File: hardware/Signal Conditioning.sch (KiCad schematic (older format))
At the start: 22 parts, among them U2 LM324, U3 LM324

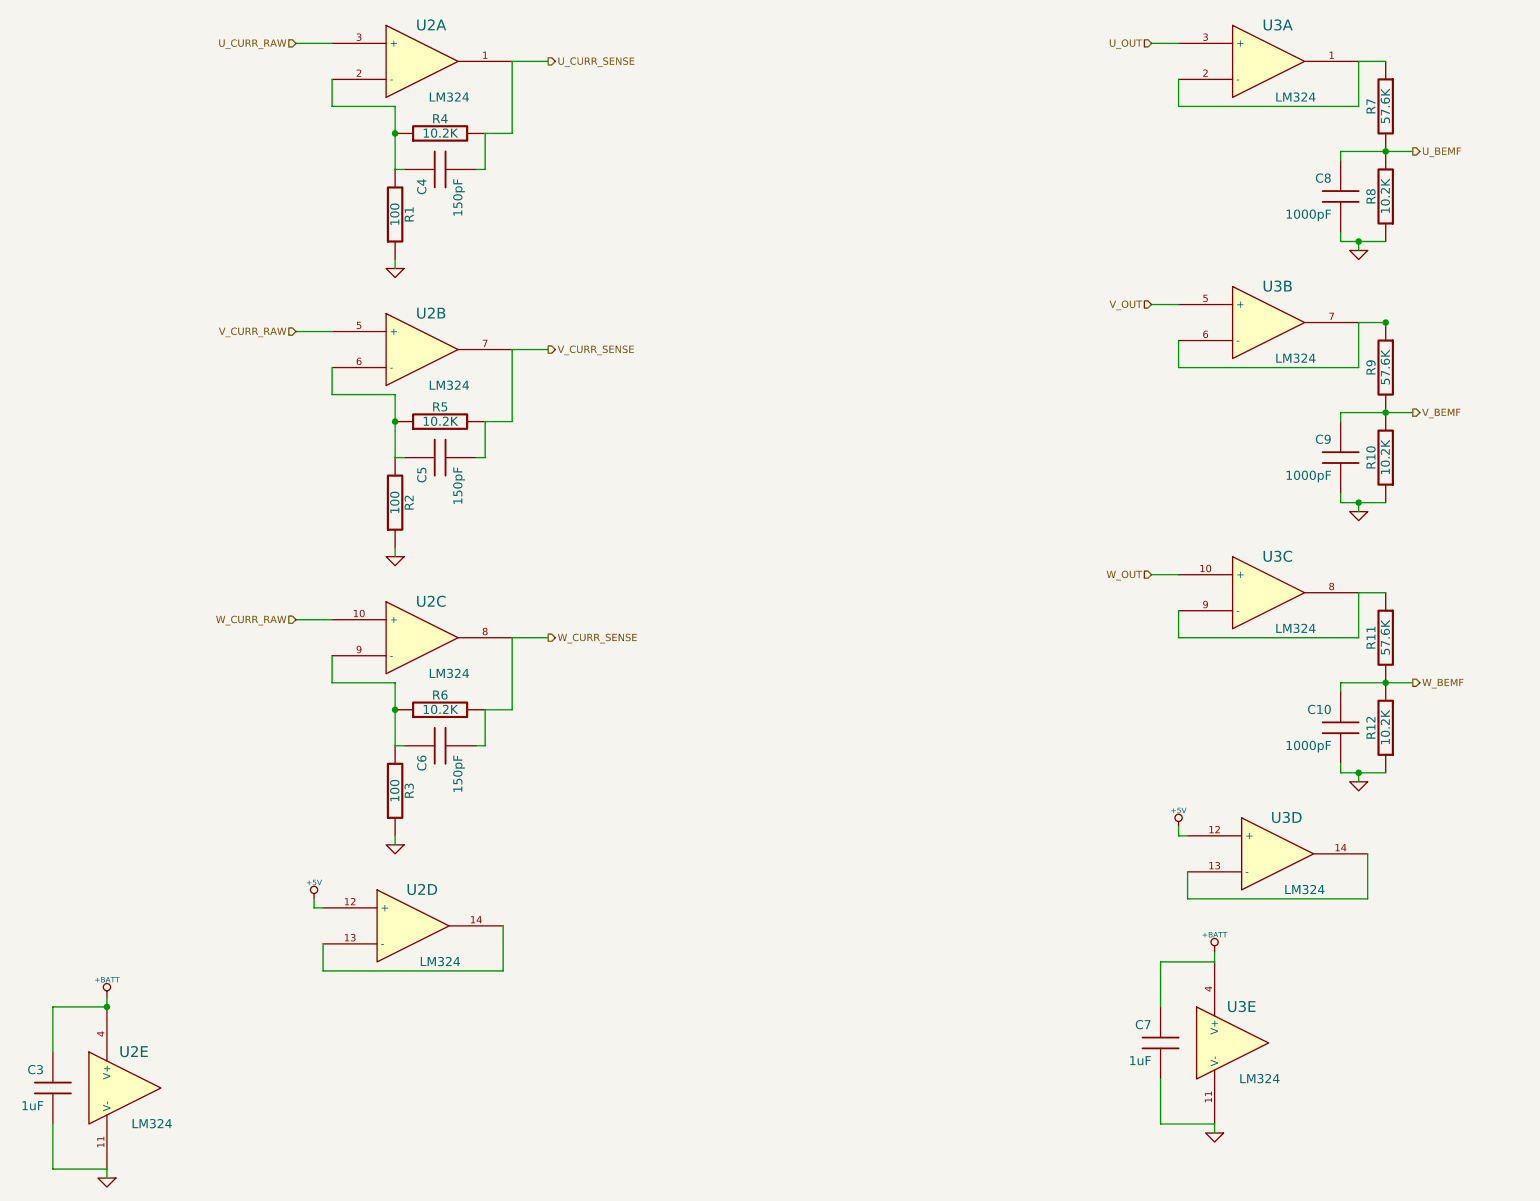
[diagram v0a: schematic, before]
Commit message: Modified schematic to use one less op-amp and a cheaper microcontroller
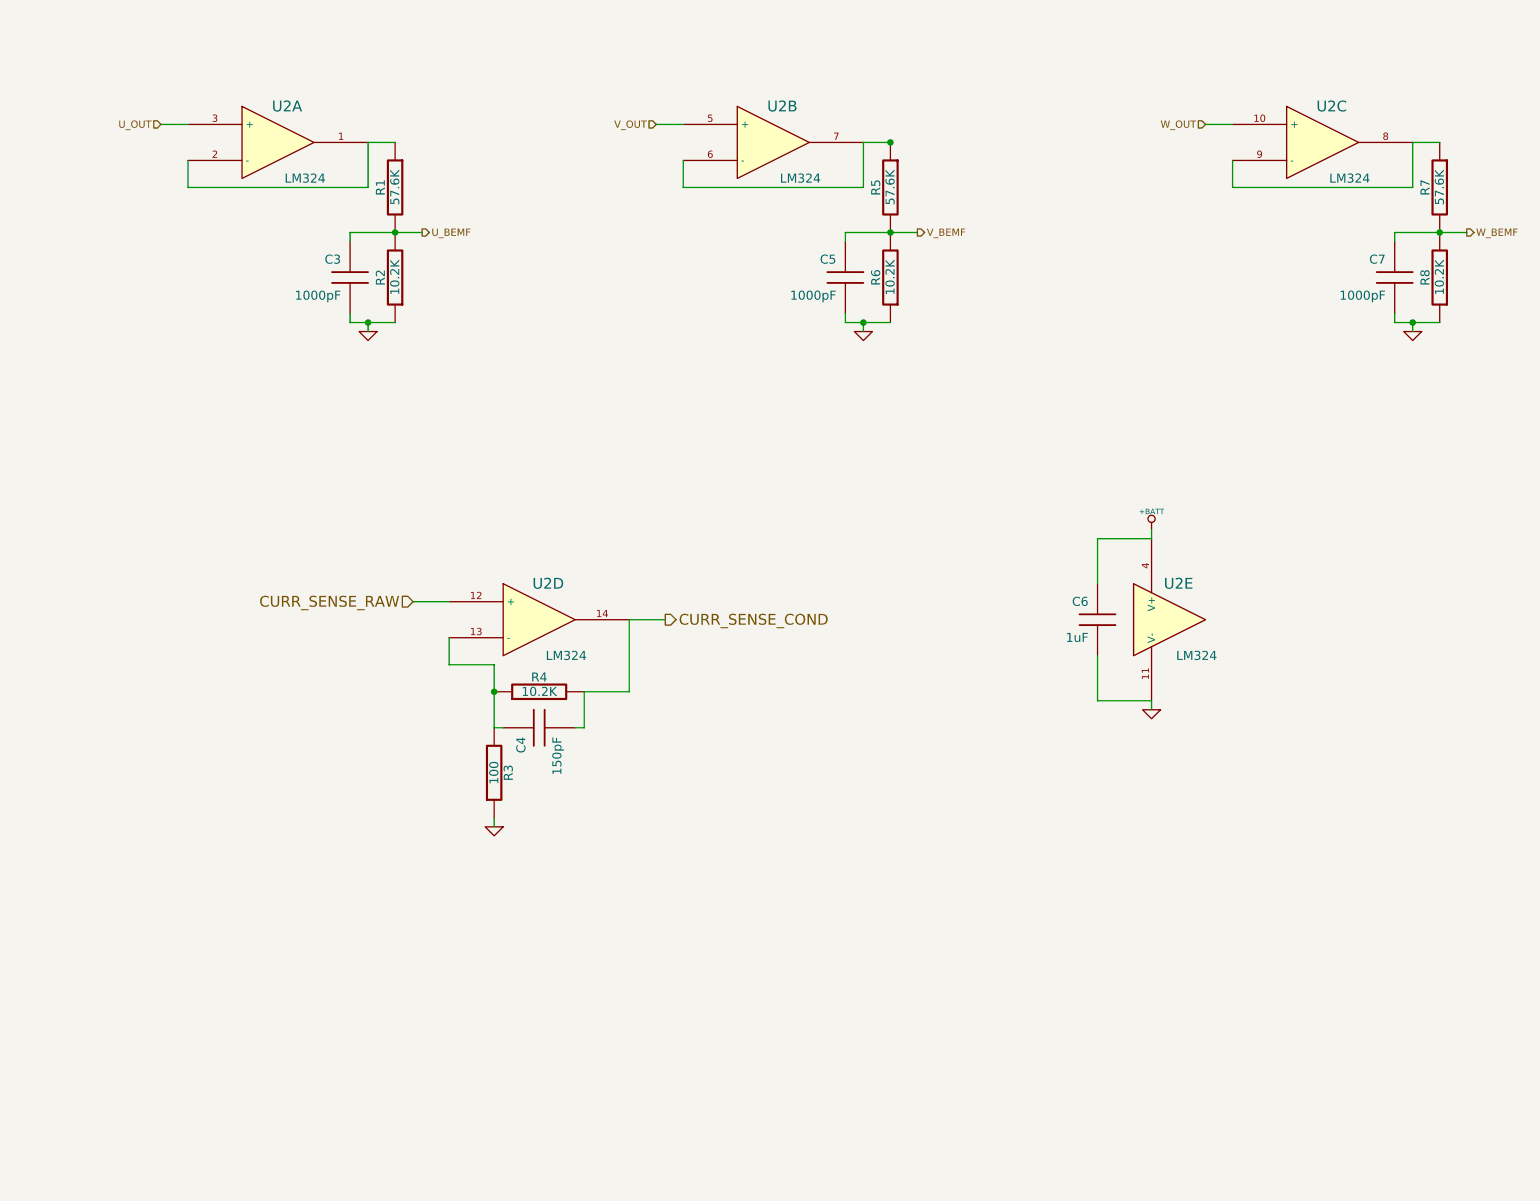
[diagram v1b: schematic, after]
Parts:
- removed C3: 1uF, 0805, symbol C
- removed C5, C6: 150pF, 0805, symbol C
- removed R2, R3: 100, 0805, symbol R
- removed R5, R6: 10.2K, 0805, symbol R
- removed U2: LM324, SOIC-14, symbol LM324
- renumbered C8 to C3, C9 to C5, C7 to C6, C10 to C7, R7 to R1, R8 to R2, R1 to R3, R9 to R5, R10 to R6, R11 to R7, R12 to R8, U3 to U2
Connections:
- net +BATT: now also U2.4 (V+); no longer U2.4 (V+)
- net GND: now also U2.11 (V-); no longer U2.11 (V-)
- net V_OUT: now also U2.5 (+); no longer U2.5 (+)
- net W_OUT: now also U2.10 (+); no longer U2.10 (+)
- net at C4.1, R3.2, R4.1: now also U2.13 (-)
- removed net +5V: U2.12 (+)
- net U_CURR_SENSE renamed CURR_SENSE_COND
- net CURR_SENSE_COND: now also U2.14
- new net: R5.1, U2.6 (-), U2.7
- new net: R7.1, U2.8, U2.9 (-)
- new net CURR_SENSE_RAW: U2.12 (+)
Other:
- moved on the sheet: C3, C4, C5, C6, C7, R1, R2, R3, R4, R5, R6, R7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

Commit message: Modified schemdatic to use a single PWM channel, similar to Atmel's app note.
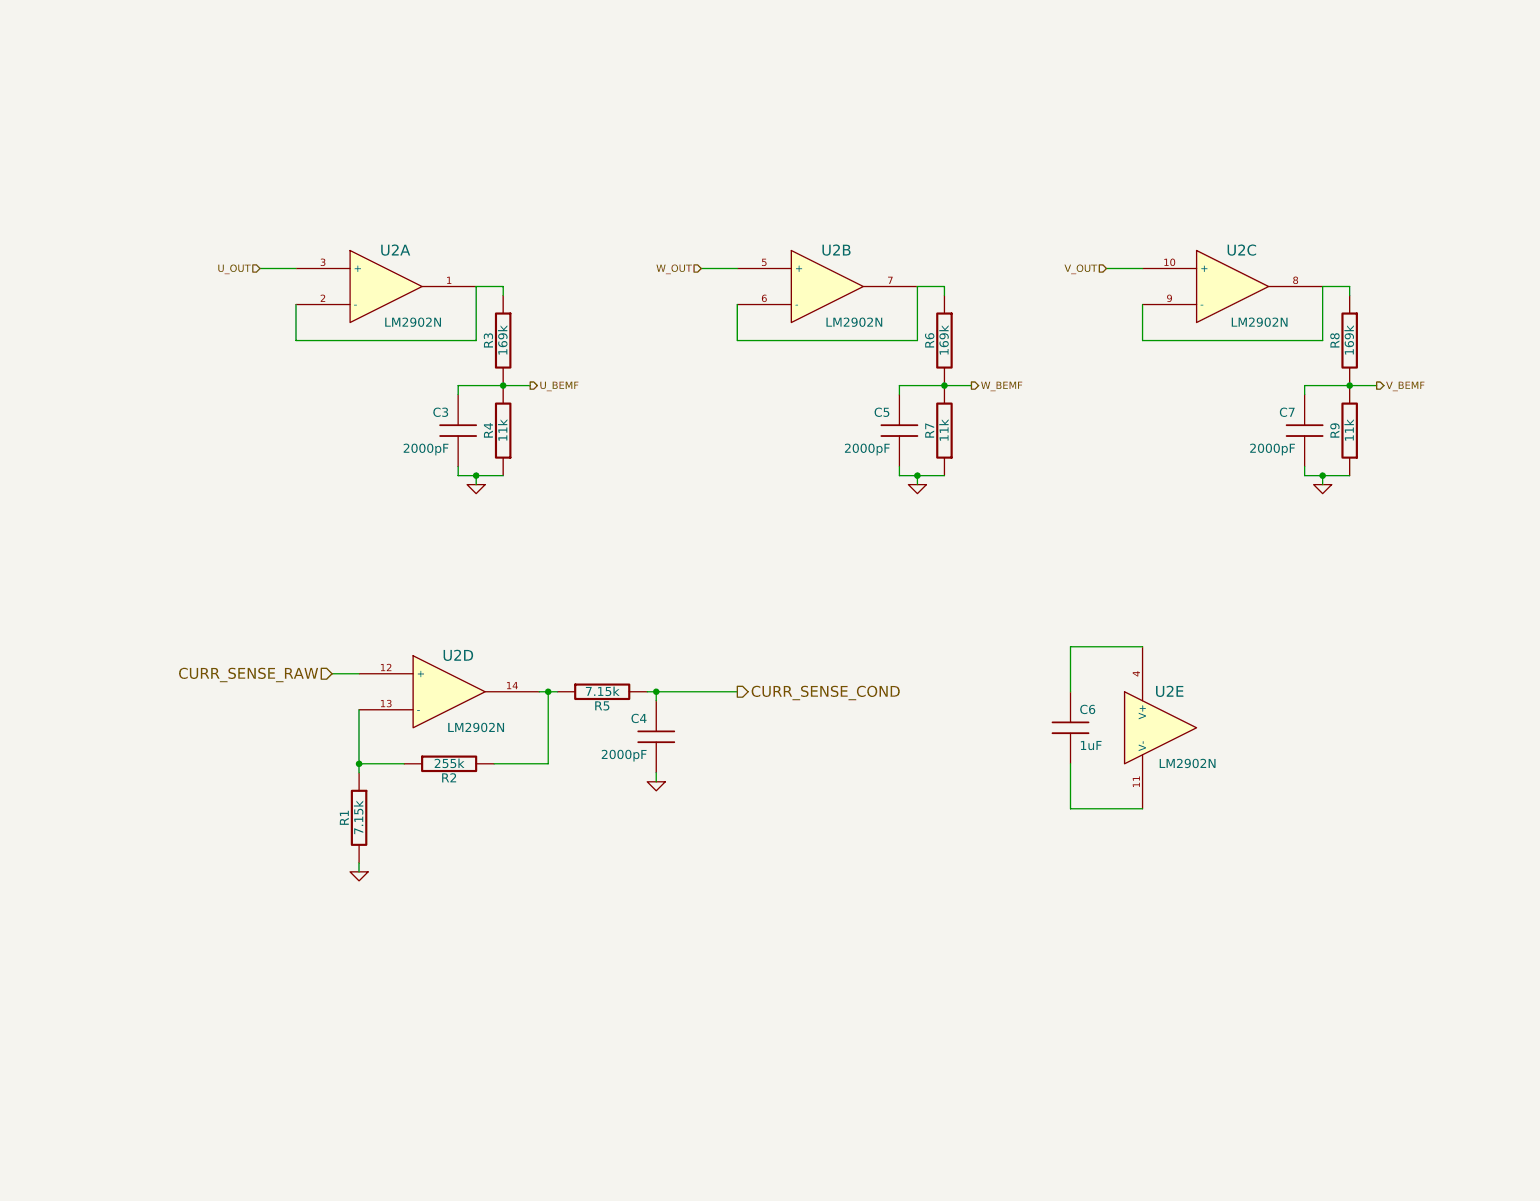
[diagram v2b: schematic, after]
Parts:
- removed R3: 100, 0805, symbol R
- removed R4: 10.2K, 0805, symbol R
- removed U2: LM324, SOIC-14, symbol LM324
- added R1, R5: 7.15k, 0805, symbol R
- added R2: 255k, 0805, symbol R
- added U2: LM2902N, symbol LM2902N
- C3: value 1000pF -> 2000pF
- C4: value 150pF -> 2000pF; Digikey P/N 1276-1828-1-ND -> 1276-1020-1-ND; Mfg P/N CL21C151JBANNNC -> CL21B102KBANNNC
- C5: renamed from C7; value 1000pF -> 2000pF
- C7: renamed from C5; value 1000pF -> 2000pF
- R3: renamed from R1; value 57.6K -> 169k
- R4: renamed from R2; value 10.2K -> 11k
- R6: renamed from R7; value 57.6K -> 169k
- R7: renamed from R8; value 10.2K -> 11k
- R8: renamed from R5; value 57.6K -> 169k
- R9: renamed from R6; value 10.2K -> 11k
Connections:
- net CURR_SENSE_COND: now also C4.1, R5.2; no longer C4.2
- net CURR_SENSE_RAW: now also U2.12 (+)
- net GND: now also C4.2, R1.2; no longer C6.2
- net U_OUT: now also U2.3 (+)
- net V_OUT: now also U2.10 (+)
- net W_OUT: now also U2.5 (+)
- net at R3.1: now also U2.1, U2.2 (-)
- net at R8.1: now also U2.8, U2.9 (-)
- net at R6.1: now also U2.6 (-), U2.7
- net +BATT: no longer names the net of C6.1
- net +BATT: now also U2.4 (V+)
- new net: R1.1, R2.1, U2.13 (-)
- new net: R2.2, R5.1, U2.14
- new net: C6.2, U2.11 (V-)
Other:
- moved on the sheet: C3, C5, C7, R3, R4, R6, R7, R8, R9

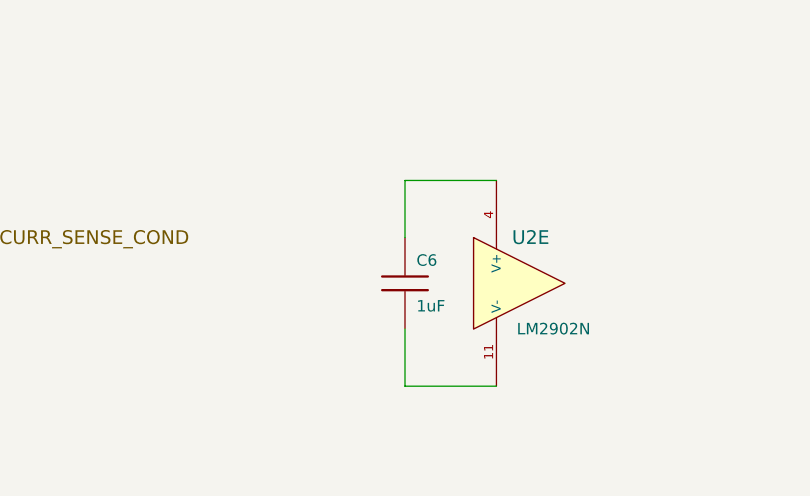
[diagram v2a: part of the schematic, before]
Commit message: Changed most parts to be through hole to simplify the initial prototype assembly
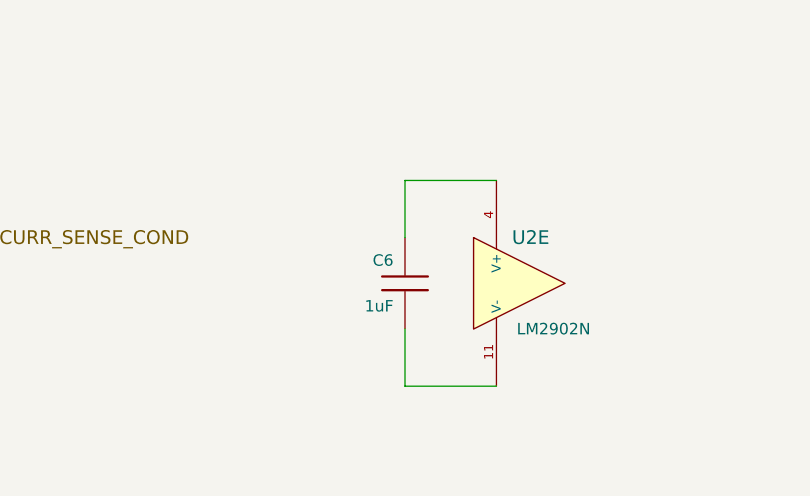
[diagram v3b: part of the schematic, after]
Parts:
- C3, C4, C5, C7: footprint 0805 -> (none); Digikey P/N 1276-1020-1-ND -> 1268PH-ND; Mfg P/N CL21B102KBANNNC -> S202M29Z5UN63L6R; Mouser P/N (none) -> 594-S202M29Z5UN63L6R
- C6: footprint 0805 -> (none); Digikey P/N 1276-3010-1-ND -> 445-8517-ND; Mfg P/N CL21F105ZBFNNNE -> FK24X7R1H105K; Mouser P/N (none) -> 810-FK24X7R1H105K
- R1, R5: footprint 0805 -> (none); Digikey P/N P56.2KCCT-ND -> 7.15KXBK-ND; Mfg P/N ERJ-6ENF5622V -> MFR-25FBF52-7K15; Mouser P/N 667-ERJ-6ENF5622V -> 603-MFR-25FBF52-7K15
- R2: footprint 0805 -> (none); Digikey P/N P56.2KCCT-ND -> 255KXBK-ND; Mfg P/N ERJ-6ENF5622V -> MFR-25FBF52-255K; Mouser P/N 667-ERJ-6ENF5622V -> 603-MFR-25FBF52-255K
- R3, R6, R8: footprint 0805 -> (none); Digikey P/N P56.2KCCT-ND -> 169KXBK-ND; Mfg P/N ERJ-6ENF5622V -> MFR-25FBF52-169K; Mouser P/N 667-ERJ-6ENF5622V -> 603-MFR-25FBF52-169K
- R4, R7, R9: footprint 0805 -> (none); Digikey P/N P10.2KCCT-ND -> 11.0KXBK-ND; Mfg P/N ERJ-6ENF1022V -> MFR-25FBF52-11K; Mouser P/N 667-ERJ-6ENF1022V -> 603-MFR-25FBF52-11K
